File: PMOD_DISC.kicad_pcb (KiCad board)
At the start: 2 copper layers, 96 x 53 mm, 150 parts, among them J1 Conn_Coaxial, J2 Conn_01x03_Male, J3 Conn_01x03_Male, J4 Conn_02x06_Odd_Even, J5 Conn_Coaxial, J6 Conn_01x03_Male, J7 Conn_01x03_Male, J8 Conn_01x04_Male, U1 LM7171xIM, U2 LM358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

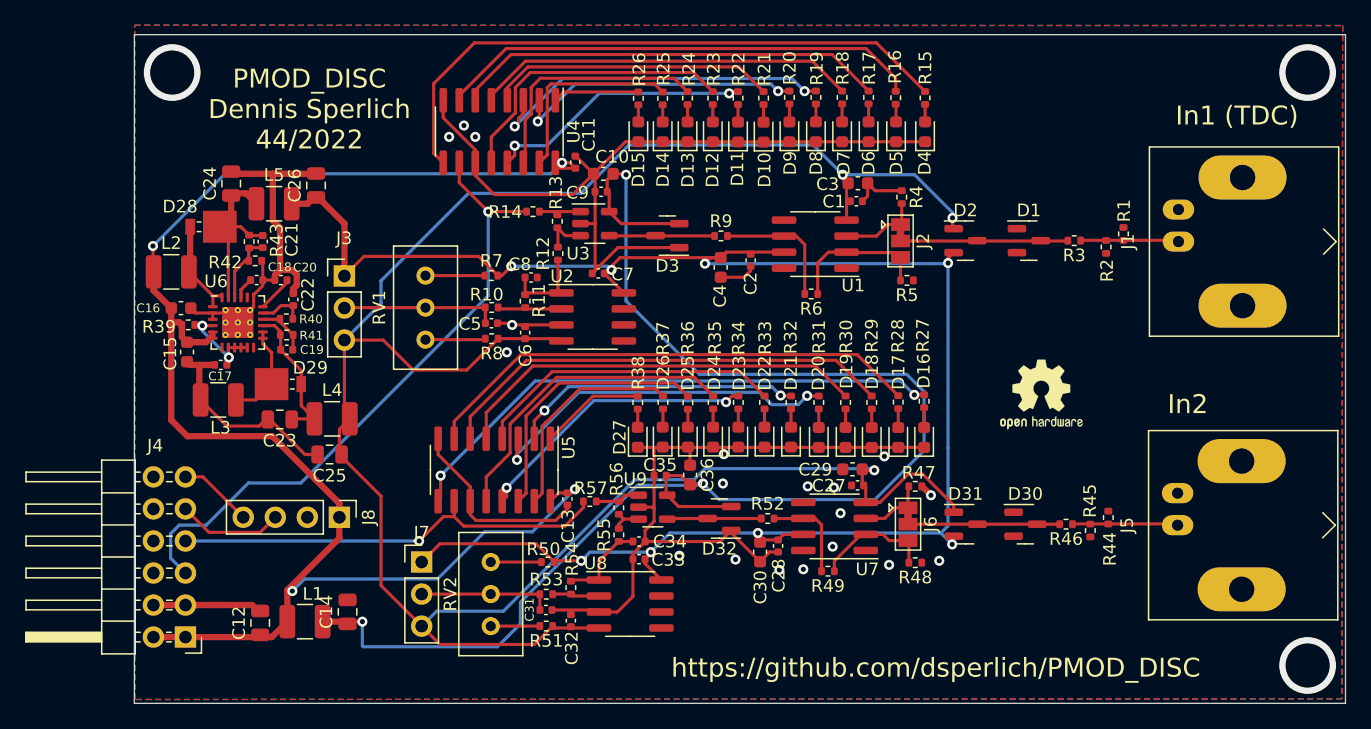
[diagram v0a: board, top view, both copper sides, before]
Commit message: add counter reset button + cleanup
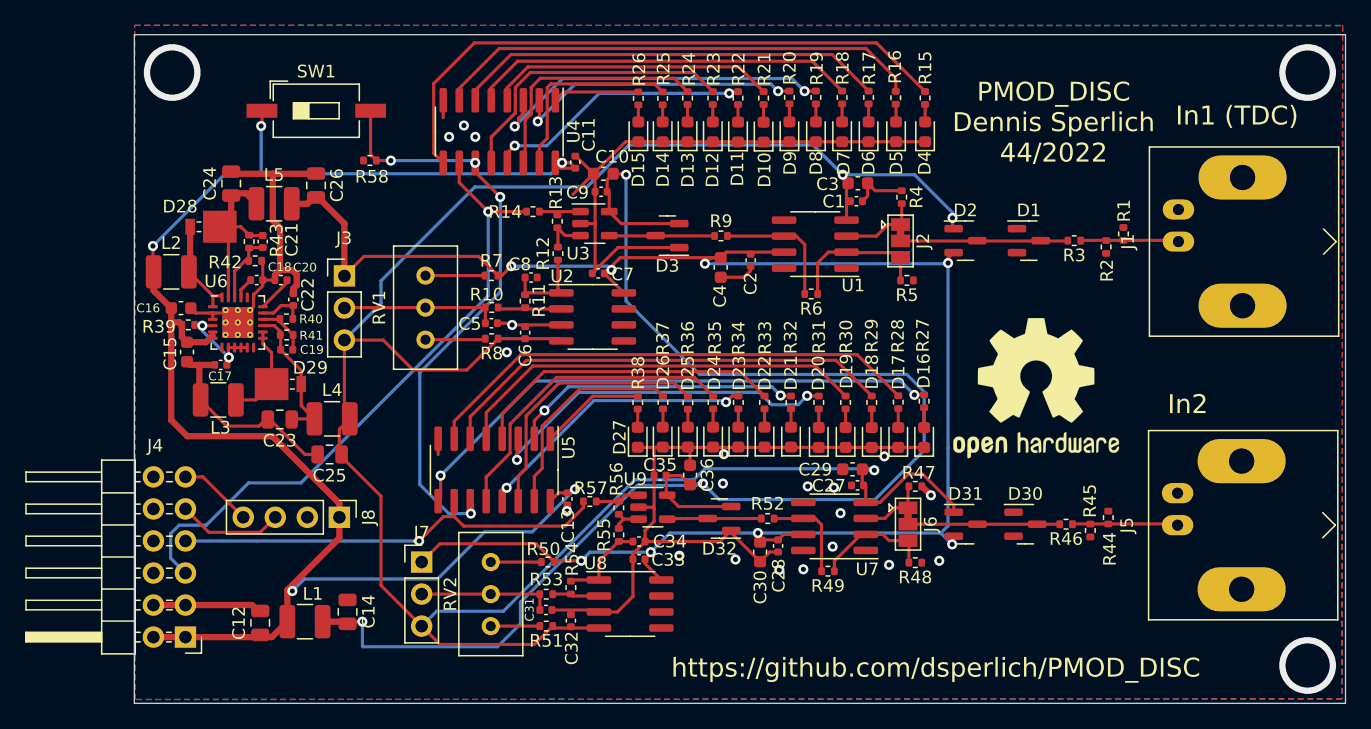
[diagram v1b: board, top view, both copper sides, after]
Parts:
- removed the REF** at (238.4, 77.0)
- added R58: 1k, Resistor_SMD:R_0402_1005Metric, F.Cu at (185.2, 58.5)
- added REF**: OSHW-Logo2_14.6x12mm_SilkScreen, Symbol:OSHW-Logo2_14.6x12mm_SilkScreen, F.Cu at (238.0, 76.5)
- added SW1: SW_Push_Dual, Button_Switch_SMD:SW_DIP_SPSTx01_Slide_6.7x4.1mm_W8.61mm_P2.54mm_LowProfile, F.Cu at (180.9, 54.5)
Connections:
- U4 pad 11: GND -> Net-(U4-Pad11)
- U5 pad 11: GND -> Net-(U4-Pad11)
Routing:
- net Net-(U4-Pad11): track 0.00 -> 47.0 mm, vias 0 -> 4
- net GND: track 204.9 -> 177.0 mm, vias 22 -> 23
- net +3.3V: track 124.6 -> 129.6 mm, vias 4 -> 5
